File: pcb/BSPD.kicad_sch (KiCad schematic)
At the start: 50 parts, among them J1 Test header, J2 T4142012121-000, Q1 AO3400A, U1 LM339, U2 LM339, U3 74HC32, U4 74HC02

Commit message: CI/CD Changes
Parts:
- C1, C2, C3, C4, C5, C6: Spice_Model 0.1u -> (none); Spice_Netlist_Enabled Y -> (none); Spice_Primitive C -> (none)
- C10, C11, C7, C8: Spice_Model 1u -> (none); Spice_Netlist_Enabled Y -> (none); Spice_Primitive C -> (none)
- C9: Spice_Model 10u -> (none); Spice_Netlist_Enabled Y -> (none); Spice_Primitive C -> (none)
- D1: Spice_Model SP0502BAHT -> (none); Spice_Netlist_Enabled N -> (none); Spice_Primitive D -> (none)
- D5: Spice_Model D_Schottky -> (none); Spice_Netlist_Enabled N -> (none); Spice_Primitive D -> (none)
- R10, R11, R12, R13, R23, R24, R25, R26, R27, R9: Spice_Model 10k -> (none); Spice_Netlist_Enabled Y -> (none); Spice_Primitive R -> (none)
- R17, R18, R19, R20, R4, R6: Spice_Model 100k -> (none); Spice_Netlist_Enabled Y -> (none); Spice_Primitive R -> (none)
- R5, R7: Spice_Model 100k -> (none); Spice_Netlist_Enabled N -> (none); Spice_Primitive R -> (none)
- U1, U2: Spice_Lib_File SPICE models/lmx39_spice.lib -> (none); Spice_Model LM339 -> (none); Spice_Netlist_Enabled Y -> (none); Spice_Primitive X -> (none)
- U3: Spice_Lib_File SPICE models/74hc32.lib -> (none); Spice_Model 74HC32_pkg -> (none); Spice_Netlist_Enabled Y -> (none); Spice_Primitive X -> (none)
- U4: Spice_Lib_File SPICE models/74hc02.lib -> (none); Spice_Model 74HC02_pkg -> (none); Spice_Netlist_Enabled Y -> (none); Spice_Primitive X -> (none)

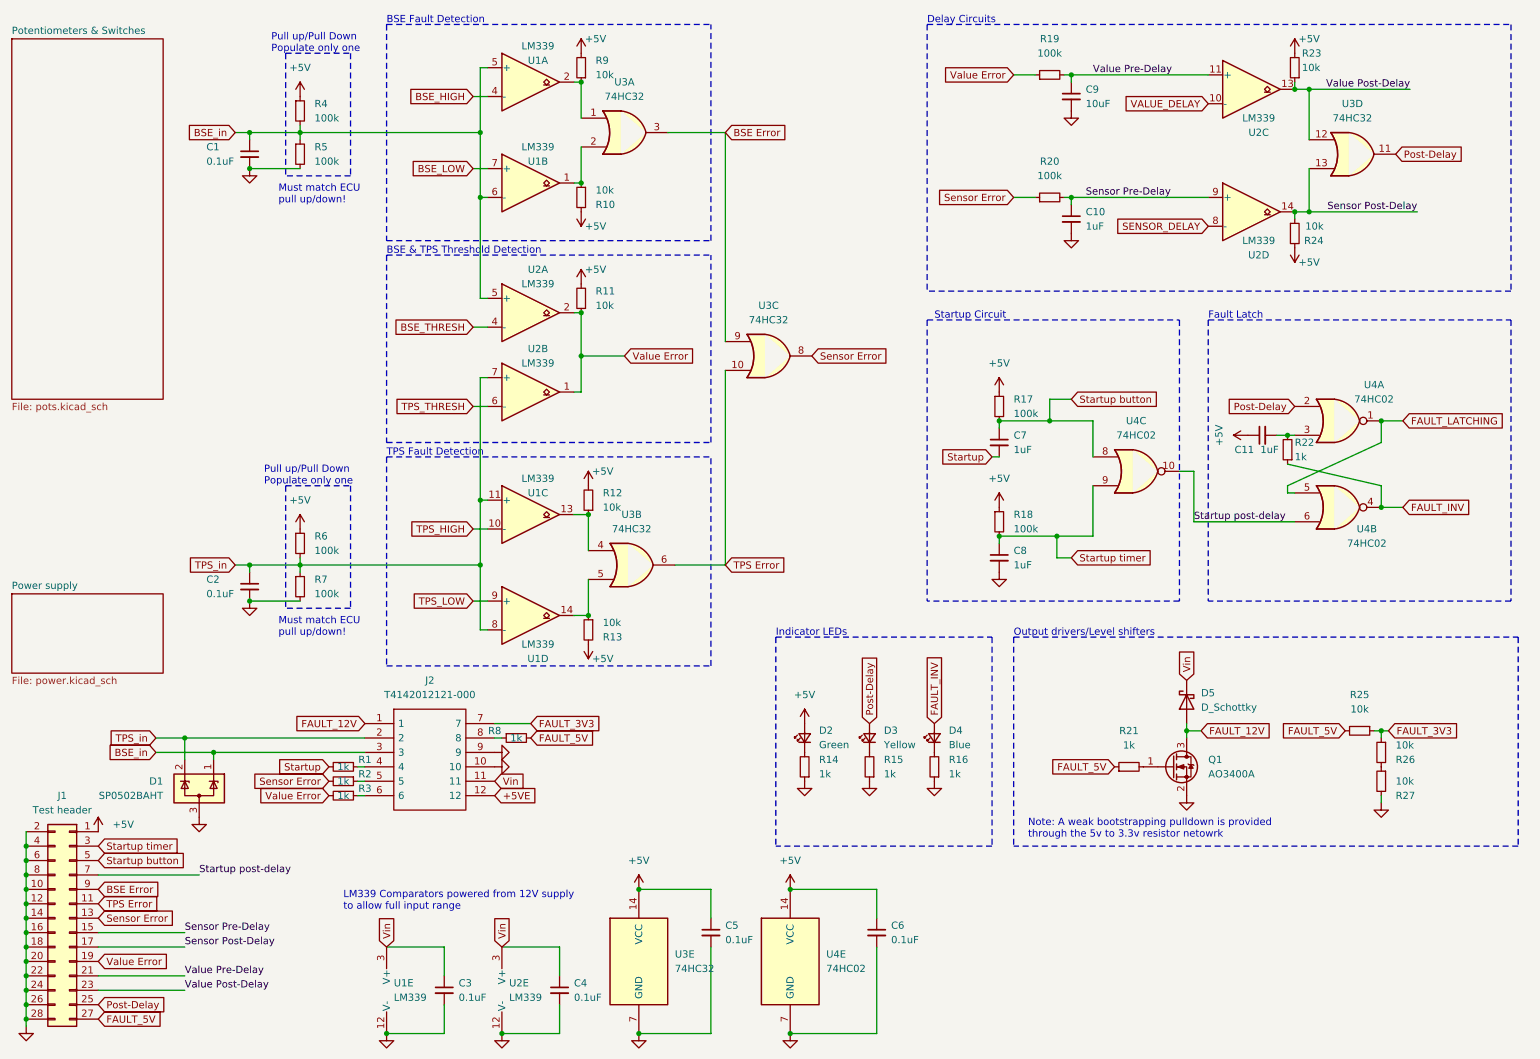
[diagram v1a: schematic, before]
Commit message: Initial Schematic and PCB changes for BR2025
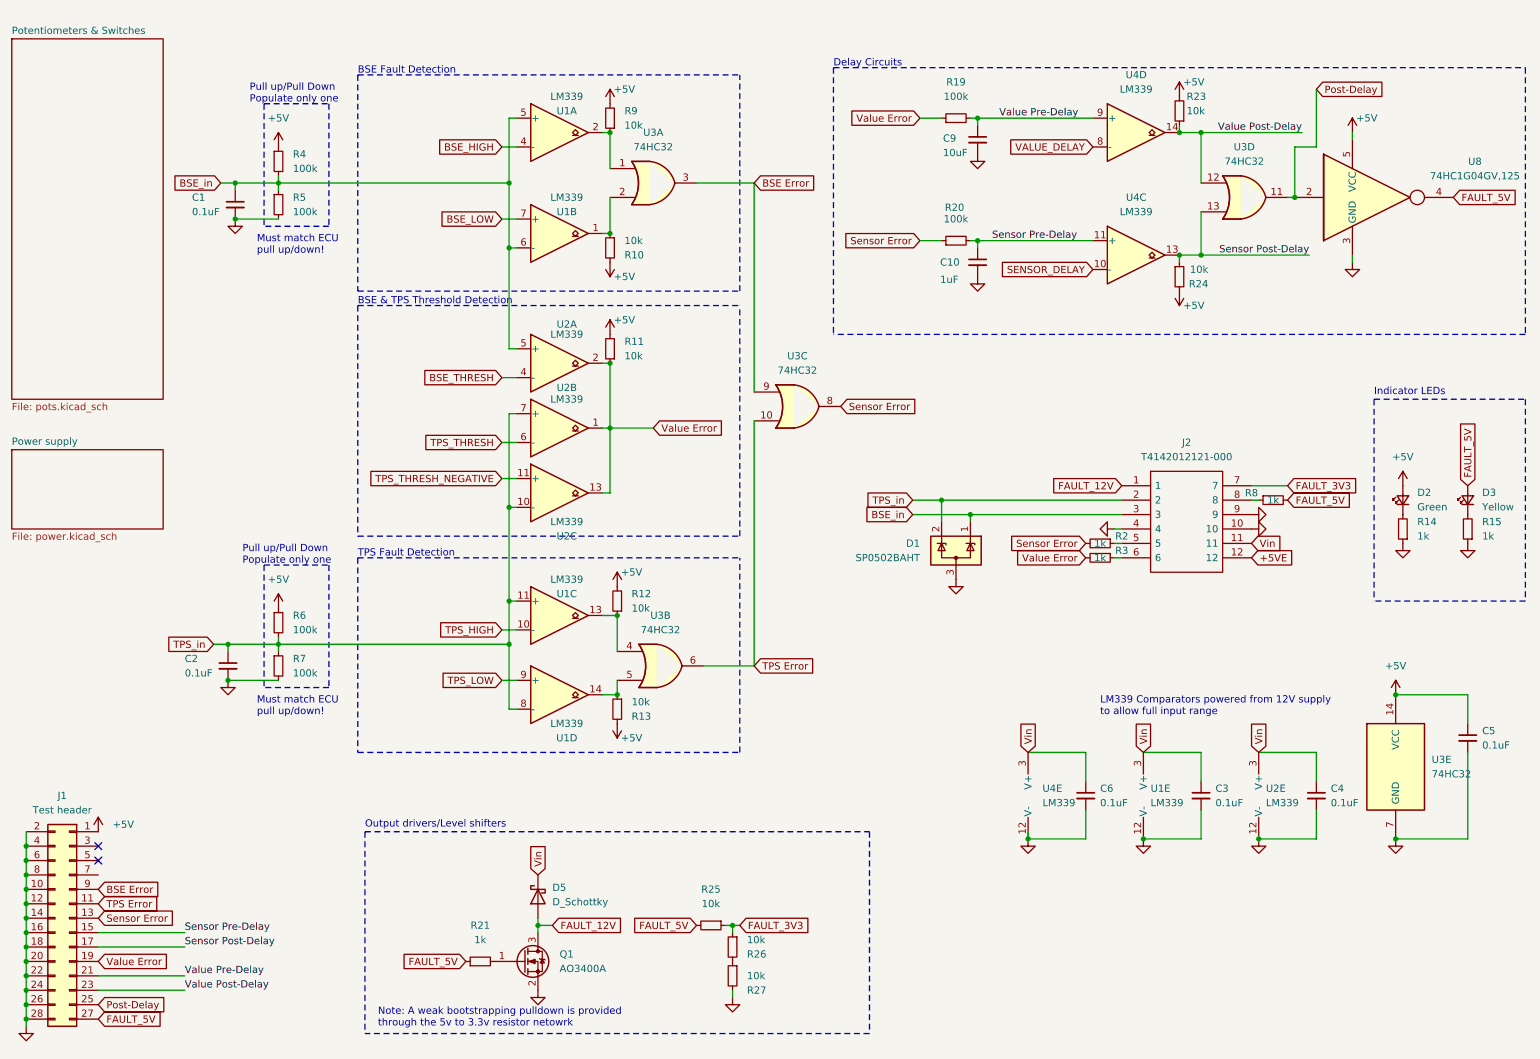
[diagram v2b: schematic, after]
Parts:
- removed C11, C7, C8: 1uF, Capacitor_SMD:C_0402_1005Metric, symbol Device:C_Small
- removed D4: Blue, LED_SMD:LED_0603_1608Metric, symbol Device:LED_Small
- removed R1, R16, R22: 1k, Resistor_SMD:R_0402_1005Metric, symbol Device:R_Small
- removed R17, R18: 100k, Resistor_SMD:R_0402_1005Metric, symbol Device:R_Small
- removed unit 4 of U2
- removed U4: 74HC02, Package_SO:SOIC-14_3.9x8.7mm_P1.27mm, symbol 74xx:74HC02
- added U4: LM339, Package_SO:SOIC-14_3.9x8.7mm_P1.27mm, symbol Comparator:LM339
- added U8: 74HC1G04GV,125, libraries:SOT23-5_FAS, symbol 74xGxx:74LVC1GU04DRL
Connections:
- net +5V: now also U8.5 (VCC); no longer C6.1
- net FAULT_5V: now also D3.2 (A), U8.4
- net GND: now also J2.4, U4.12 (V-), U8.3 (GND)
- net Post-Delay: now also U8.2; no longer D3.2 (A)
- net SENSOR_DELAY: now also U4.10 (-)
- net Sensor Post-Delay: now also U4.13
- net Sensor Pre-Delay: now also U4.11 (+)
- net TPS_in: now also U2.10 (-)
- net VALUE_DELAY: now also U4.8 (-); no longer U2.10 (-)
- net Value Error: now also U2.13
- net Value Post-Delay: now also U4.14; no longer U2.13
- net Value Pre-Delay: now also U4.9 (+); no longer U2.11 (+)
- net Vin: now also C6.1, U4.3 (V+)
- net Startup button: no longer names the net of J1.5 (Pin_5)
- net Startup post-delay: no longer names the net of J1.7 (Pin_7)
- net Startup timer: no longer names the net of J1.3 (Pin_3)
- new net TPS_THRESH_NEGATIVE: U2.11 (+)
- no-connect marks 0 -> 2
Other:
- note removed: "Fault Latch"
- note removed: "Startup Circuit"
- moved on the sheet: C1, C10, C2, C3, C4, C5, C9, D1, D2, D3, D5, J2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
